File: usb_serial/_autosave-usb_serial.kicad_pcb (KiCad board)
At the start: 2 copper layers, 17 parts, among them P1 USB_OTG, P2 CONN_01X04, P3 CONN_01X04, Q1 S8050, Q2 S8050, U1 CH340G, X1 CRYSTAL_SMD

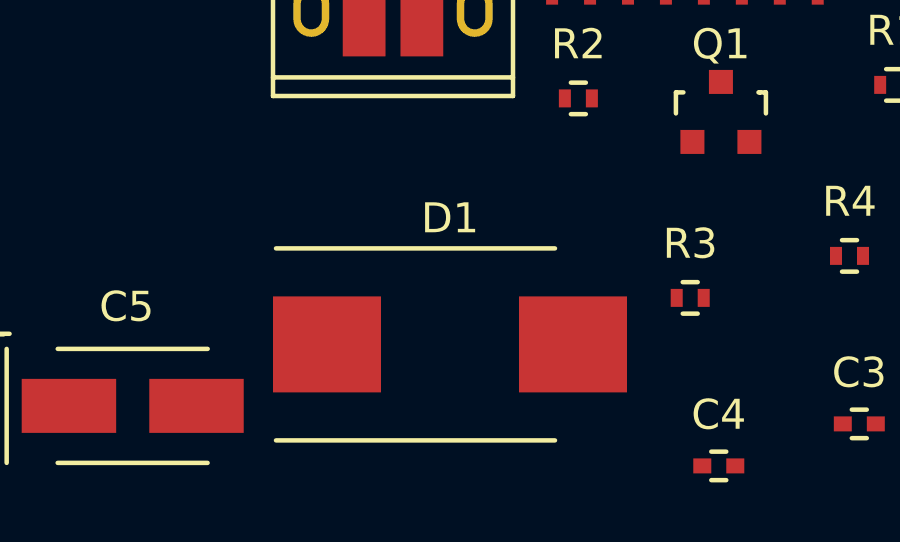
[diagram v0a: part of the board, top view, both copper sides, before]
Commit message: Fixes in usb footprints. usb/README.md added.
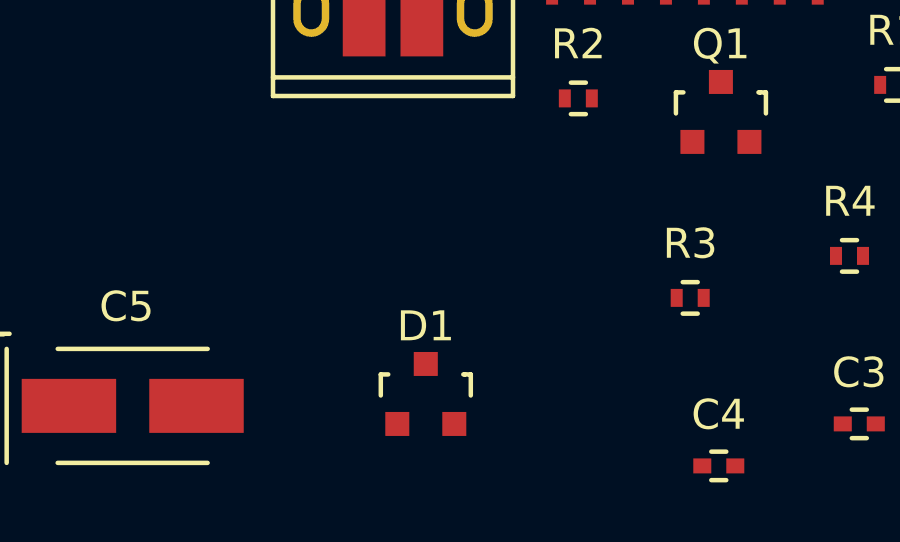
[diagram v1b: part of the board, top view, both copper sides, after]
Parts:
- C2: value C -> 100nF
- D1: value D_Schottky -> D_Schottky_x2_ACom_AKK; footprint Diodes_SMD:DO-214AB_Handsoldering -> TO_SOT_Packages_SMD:SOT-23
- moved D1 1.84 mm to (190.6, 121.7)
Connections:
- D1 pad 1: +5V -> +5P
- D1 pad 2: +5P -> Net-(D1-Pad2)
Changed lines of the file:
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@@
     (zones 0)
     (modules 17)
-    (nets 25)
+    (nets 26)
   )
   (page A4)
@@
   (net 23 "Net-(U1-Pad10)")
   (net 24 "Net-(U1-Pad9)")
+  (net 25 "Net-(D1-Pad2)")
   (net_class Default "This is the default net class."
     (clearance 0.2)
@@
     (add_net "Net-(C2-Pad1)")
     (add_net "Net-(C3-Pad1)")
+    (add_net "Net-(D1-Pad2)")
     (add_net "Net-(P1-Pad4)")
     (add_net "Net-(Q1-Pad2)")
@@
       (effects (font (size 1 1) (thickness 0.15)))
     )
-    (fp_text value C (at 0 1.7) (layer F.Fab)
+    (fp_text value 100nF (at 0 1.7) (layer F.Fab)
       (effects (font (size 1 1) (thickness 0.15)))
     )
@@
       (at (xyz 0 0 0))
       (scale (xyz 1 1 1))
-      (rotate (xyz 0 0 180))
-    )
-  )
-  (module Diodes_SMD:DO-214AB_Handsoldering (layer F.Cu)
-    (at 191.387001 120.079)
-    (descr "Jedec DO-214AB diode package. Designed according to Fairchild SS32 datasheet.")
-    (tags "DO-214AB diode Handsoldering")
-    (attr smd)
-    (fp_text reference D1 (at 0 -4.2) (layer F.SilkS)
-      (effects (font (size 1 1) (thickness 0.15)))
-    )
-    (fp_text value D_Schottky (at 0 4.6) (layer F.Fab)
-      (effects (font (size 1 1) (thickness 0.15)))
-    )
-    (fp_line (start -6.15 -3.45) (end 6.15 -3.45) (layer F.CrtYd) (width 0.05))
-    (fp_line (start 6.15 -3.45) (end 6.15 3.45) (layer F.CrtYd) (width 0.05))
-    (fp_line (start 6.15 3.45) (end -6.15 3.45) (layer F.CrtYd) (width 0.05))
-    (fp_line (start -6.15 3.45) (end -6.15 -3.45) (layer F.CrtYd) (width 0.05))
-    (fp_line (start 3.5 3.2) (end -5.8 3.2) (layer F.SilkS) (width 0.15))
-    (fp_line (start -5.8 -3.2) (end 3.5 -3.2) (layer F.SilkS) (width 0.15))
-    (pad 2 smd rect (at 4.1 0) (size 3.6 3.2) (layers F.Cu F.Paste F.Mask)
-      (net 6 +5P))
-    (pad 1 smd rect (at -4.1 0) (size 3.6 3.2) (layers F.Cu F.Paste F.Mask)
-      (net 5 +5V))
-    (model Diodes_SMD.3dshapes/DO-214AB_Handsoldering.wrl
-      (at (xyz 0 0 0))
-      (scale (xyz 0.39 0.39 0.39))
       (rotate (xyz 0 0 180))
     )
@@
       (at (xyz 0 0 0))
       (scale (xyz 1 1 1))
+      (rotate (xyz 0 0 0))
+    )
+  )
+  (module TO_SOT_Packages_SMD:SOT-23 (layer F.Cu)
+    (at 190.58 121.73)
+    (descr "SOT-23, Standard")
+    (tags SOT-23)
+    (attr smd)
+    (fp_text reference D1 (at 0 -2.25) (layer F.SilkS)
+      (effects (font (size 1 1) (thickness 0.15)))
+    )
+    (fp_text value D_Schottky_x2_ACom_AKK (at 0 2.3) (layer F.Fab)
+      (effects (font (size 1 1) (thickness 0.15)))
+    )
+    (fp_line (start -1.65 -1.6) (end 1.65 -1.6) (layer F.CrtYd) (width 0.05))
+    (fp_line (start 1.65 -1.6) (end 1.65 1.6) (layer F.CrtYd) (width 0.05))
+    (fp_line (start 1.65 1.6) (end -1.65 1.6) (layer F.CrtYd) (width 0.05))
+    (fp_line (start -1.65 1.6) (end -1.65 -1.6) (layer F.CrtYd) (width 0.05))
+    (fp_line (start 1.29916 -0.65024) (end 1.2509 -0.65024) (layer F.SilkS) (width 0.15))
+    (fp_line (start -1.49982 0.0508) (end -1.49982 -0.65024) (layer F.SilkS) (width 0.15))
+    (fp_line (start -1.49982 -0.65024) (end -1.2509 -0.65024) (layer F.SilkS) (width 0.15))
+    (fp_line (start 1.29916 -0.65024) (end 1.49982 -0.65024) (layer F.SilkS) (width 0.15))
+    (fp_line (start 1.49982 -0.65024) (end 1.49982 0.0508) (layer F.SilkS) (width 0.15))
+    (pad 1 smd rect (at -0.95 1.00076) (size 0.8001 0.8001) (layers F.Cu F.Paste F.Mask)
+      (net 6 +5P))
+    (pad 2 smd rect (at 0.95 1.00076) (size 0.8001 0.8001) (layers F.Cu F.Paste F.Mask)
+      (net 25 "Net-(D1-Pad2)"))
+    (pad 3 smd rect (at 0 -0.99822) (size 0.8001 0.8001) (layers F.Cu F.Paste F.Mask)
+      (net 5 +5V))
+    (model TO_SOT_Packages_SMD.3dshapes/SOT-23.wrl
+      (at (xyz 0 0 0))
+      (scale (xyz 1 1 1))
